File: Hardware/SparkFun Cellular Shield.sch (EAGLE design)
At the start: 30 parts, among them U1 ARDUINO_R3_SHIELD, U2 SPX29302, U3 SM5100B

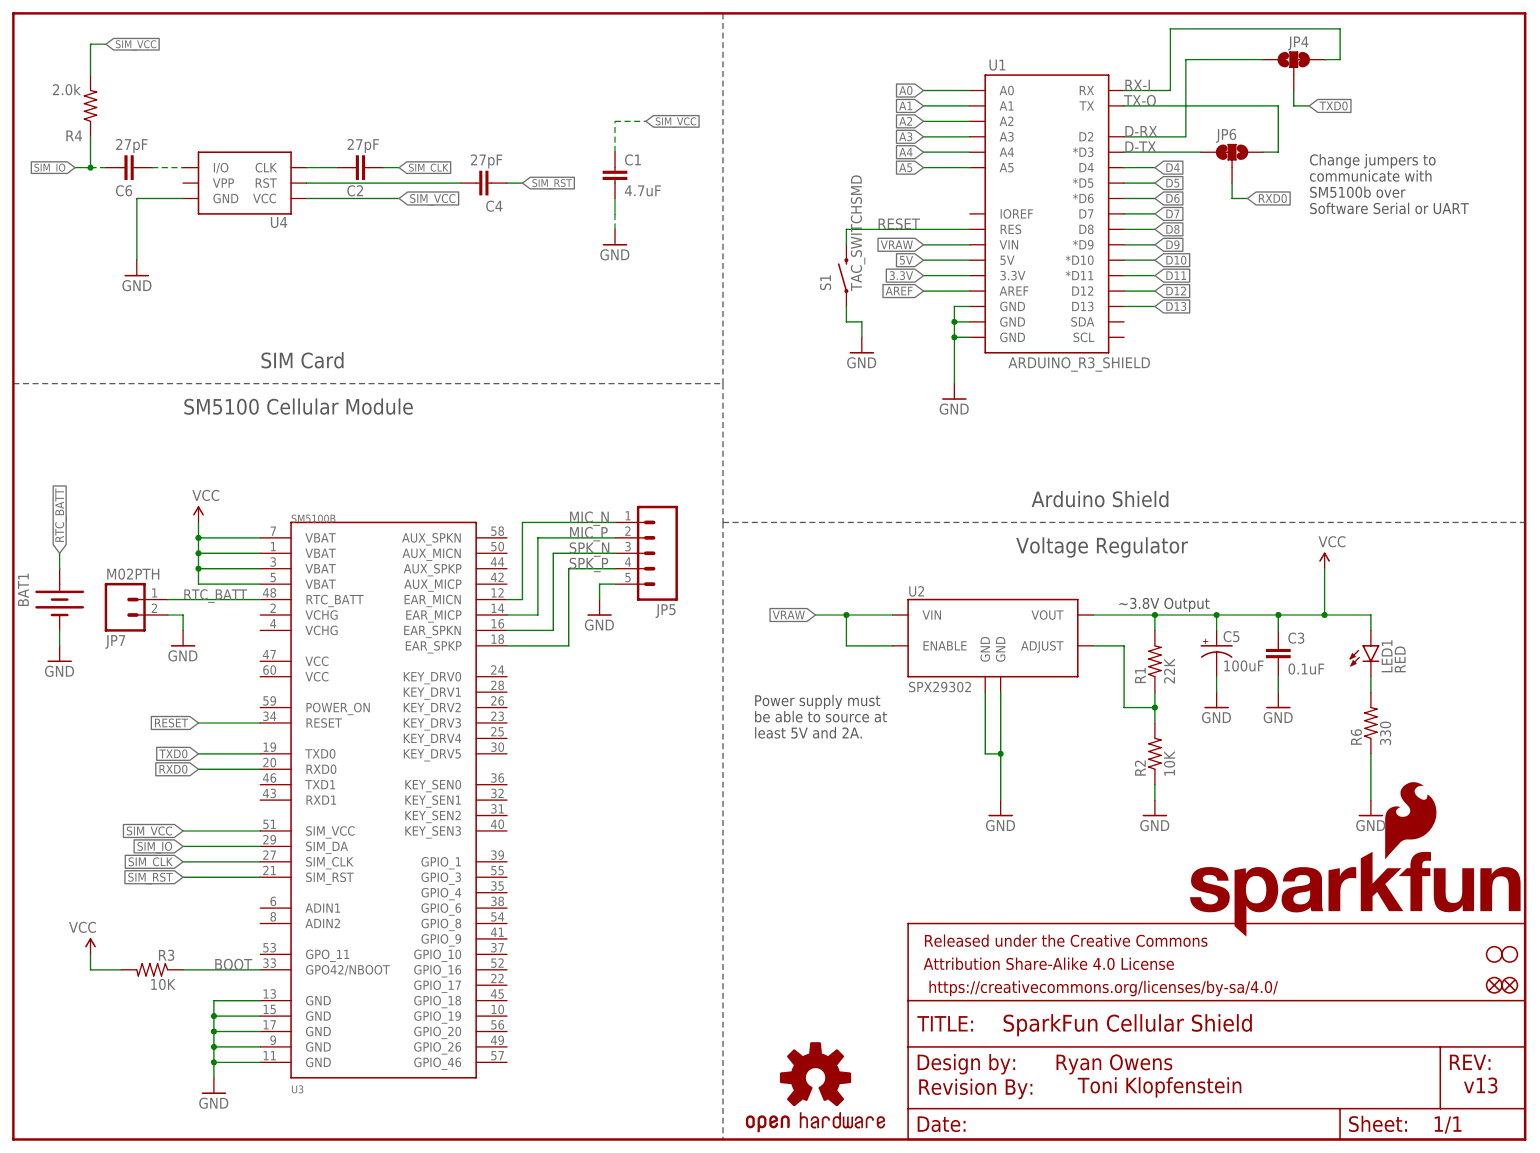
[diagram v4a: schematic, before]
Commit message: Adding fixes from QC checklist
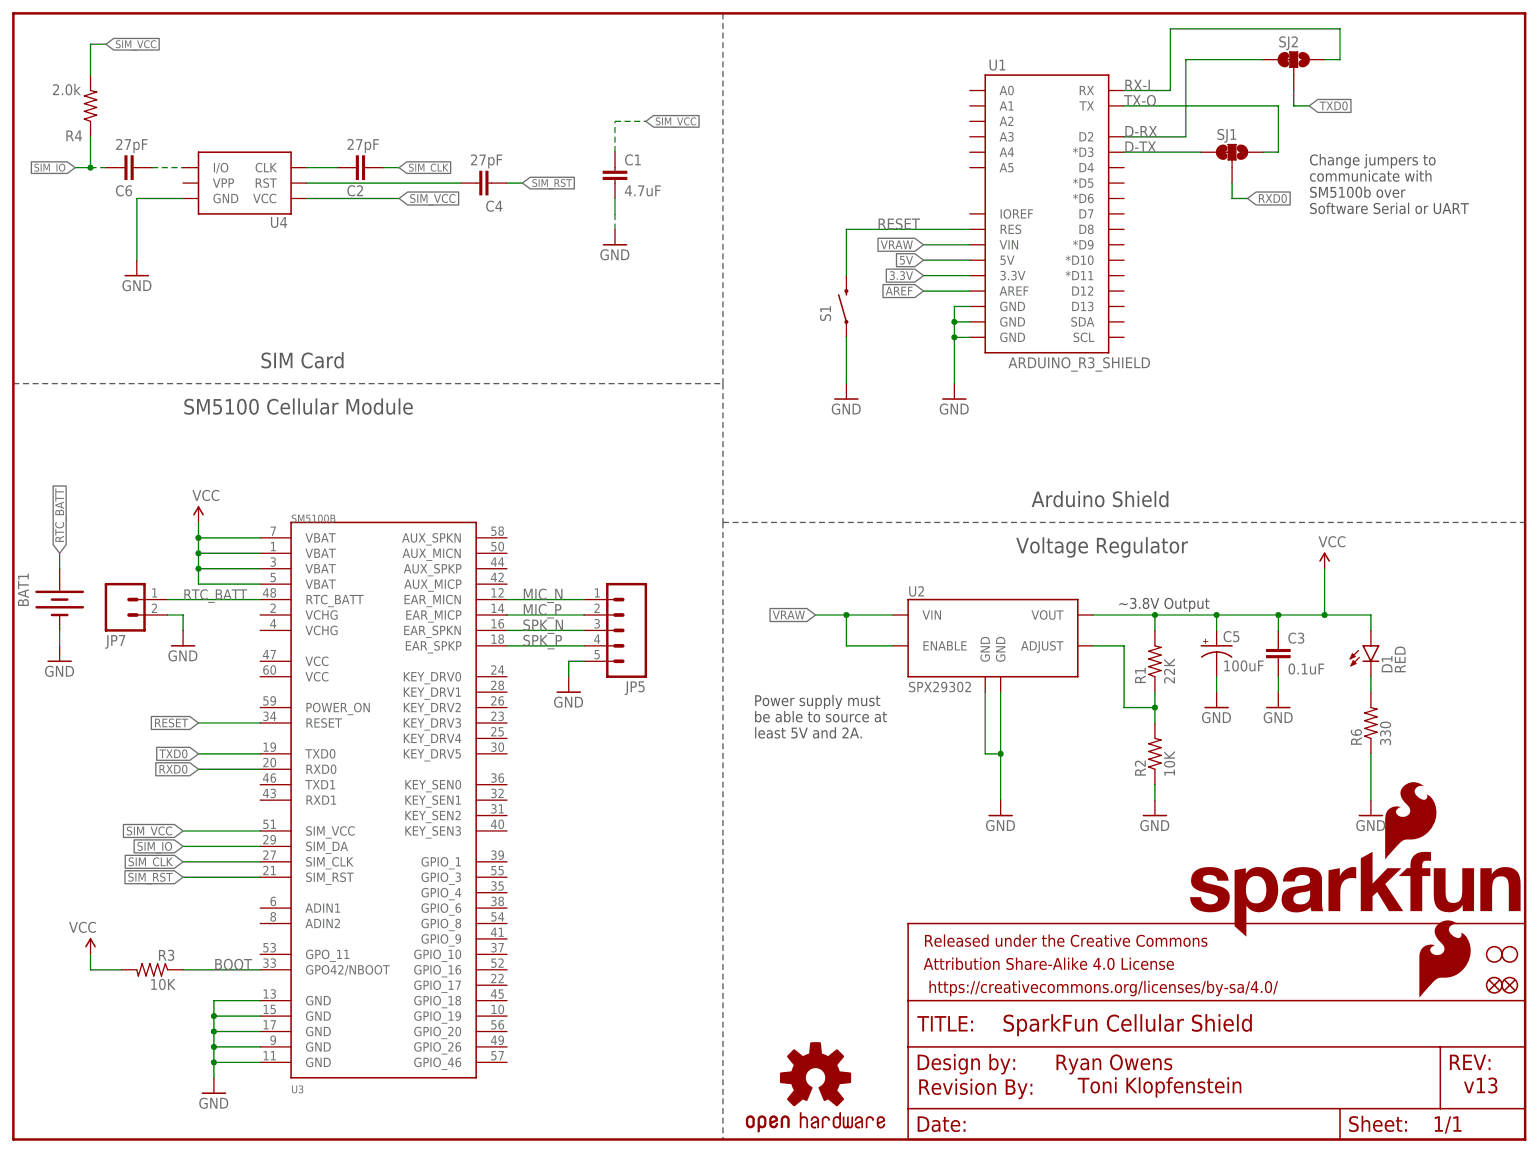
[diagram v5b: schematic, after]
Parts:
- added LOGO2: SFE_LOGO_FLAME.1_INCH, SparkFun-Aesthetics:SFE_LOGO_FLAME.1_INCH
- BAT1: device SparkFun-Electromechanical:BATTERY20PTH -> SparkFun-Electromechanical:BATTERY20SMD
- renumbered JP4 to SJ2, JP6 to SJ1, LED1 to D1
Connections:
- removed net A0: U1.A0
- removed net A1: U1.A1
- removed net A2: U1.A2
- removed net A3: U1.A3
- removed net A4: U1.A4
- removed net A5: U1.A5
- removed net D10: U1.*D10
- removed net D11: U1.*D11
- removed net D12: U1.D12
- removed net D13: U1.D13
- removed net D4: U1.D4
- removed net D5: U1.*D5
- removed net D6: U1.*D6
- removed net D7: U1.D7
- removed net D8: U1.D8
- removed net D9: U1.*D9
- net D-RX: now also SJ2.3; no longer SJ2.1
- net RX-I: now also SJ2.1; no longer SJ2.3
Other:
- moved on the sheet: JP5, S1
